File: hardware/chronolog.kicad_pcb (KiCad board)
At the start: 2 copper layers, 100 x 50 mm, 92 parts, among them J1 DC-005-5A-2.0, J2 B4B-XH-A, J3 B-2100S04P-A110, J4 U254-051N-4BH806, Q1 BSS138, Q2 BSS138, Q3 BC817-40LT1G, U1 AP63205WU-7, U2 STM32F072CBT6, U3 AP2114H-3.3TRG1, U4 USBLC6-2SC6, U5 W25Q32JVSNIQ, U6 LM75BD, U7 ESP-01, U8 WC1602A, U9 PCF8574T, Y1 32.768kHz

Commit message: hardware(feat): configure board stackup and design rules
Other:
- copper layers 2 -> 4
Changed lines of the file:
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@@
 	(generator_version "9.0")
 	(general
-		(thickness 1.6)
+		(thickness 1.6062)
 		(legacy_teardrops no)
 	)
@@
 	(layers
 		(0 "F.Cu" signal)
+		(4 "In1.Cu" signal)
+		(6 "In2.Cu" signal)
 		(2 "B.Cu" signal)
 		(9 "F.Adhes" user "F.Adhesive")
@@
 	)
 	(setup
+		(stackup
+			(layer "F.SilkS"
+				(type "Top Silk Screen")
+			)
+			(layer "F.Paste"
+				(type "Top Solder Paste")
+			)
+			(layer "F.Mask"
+				(type "Top Solder Mask")
+				(thickness 0.01)
+			)
+			(layer "F.Cu"
+				(type "copper")
+				(thickness 0.035)
+			)
+			(layer "dielectric 1"
+				(type "prepreg")
+				(thickness 0.2104)
+				(material "FR4")
+				(epsilon_r 4.5)
+				(loss_tangent 0.02)
+			)
+			(layer "In1.Cu"
+				(type "copper")
+				(thickness 0.0152)
+			)
+			(layer "dielectric 2"
+				(type "core")
+				(thickness 1.065)
+				(material "FR4")
+				(epsilon_r 4.5)
+				(loss_tangent 0.02)
+			)
+			(layer "In2.Cu"
+				(type "copper")
+				(thickness 0.0152)
+			)
+			(layer "dielectric 3"
+				(type "prepreg")
+				(thickness 0.2104)
+				(material "FR4")
+				(epsilon_r 4.5)
+				(loss_tangent 0.02)
+			)
+			(layer "B.Cu"
+				(type "copper")
+				(thickness 0.035)
+			)
+			(layer "B.Mask"
+				(type "Bottom Solder Mask")
+				(thickness 0.01)
+			)
+			(layer "B.Paste"
+				(type "Bottom Solder Paste")
+			)
+			(layer "B.SilkS"
+				(type "Bottom Silk Screen")
+			)
+			(copper_finish "None")
+			(dielectric_constraints no)
+		)
 		(pad_to_mask_clearance 0)
 		(allow_soldermask_bridges_in_footprints no)

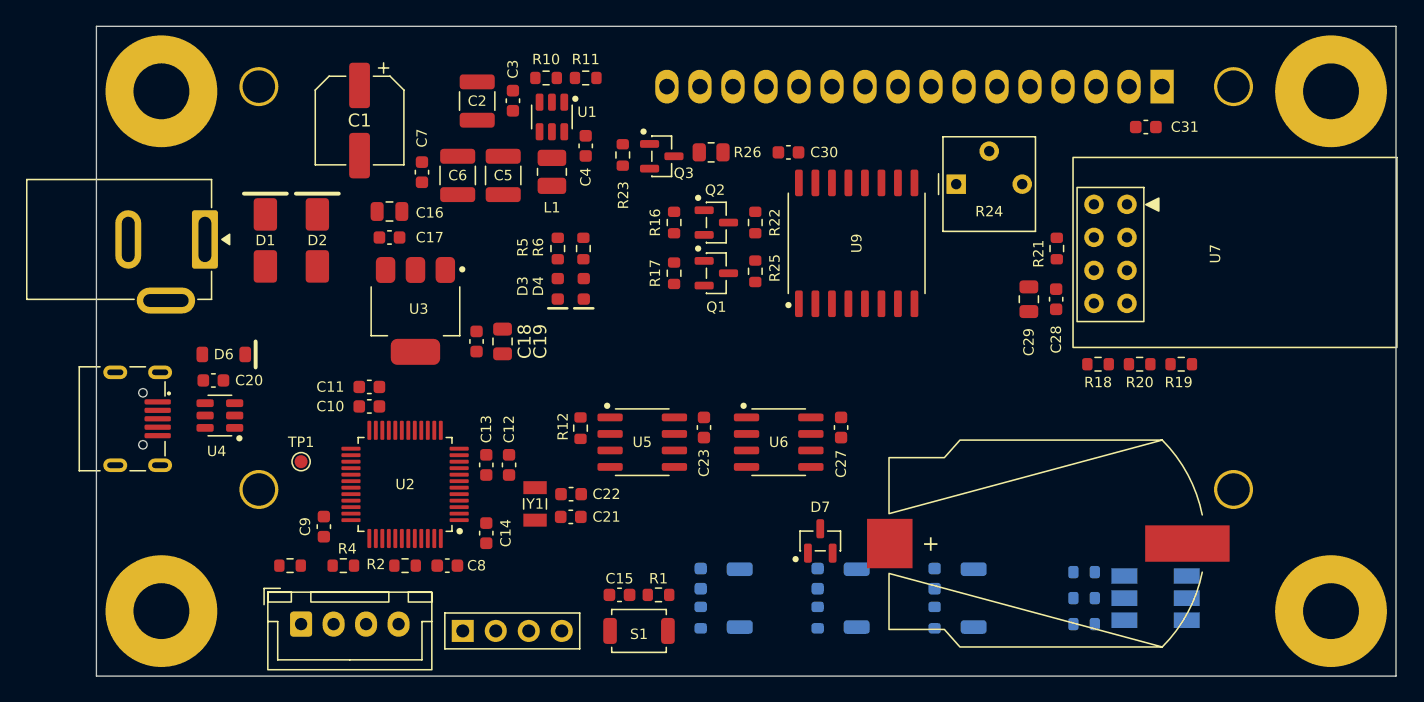
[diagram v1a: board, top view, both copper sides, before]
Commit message: hardware(feat): route simple connections
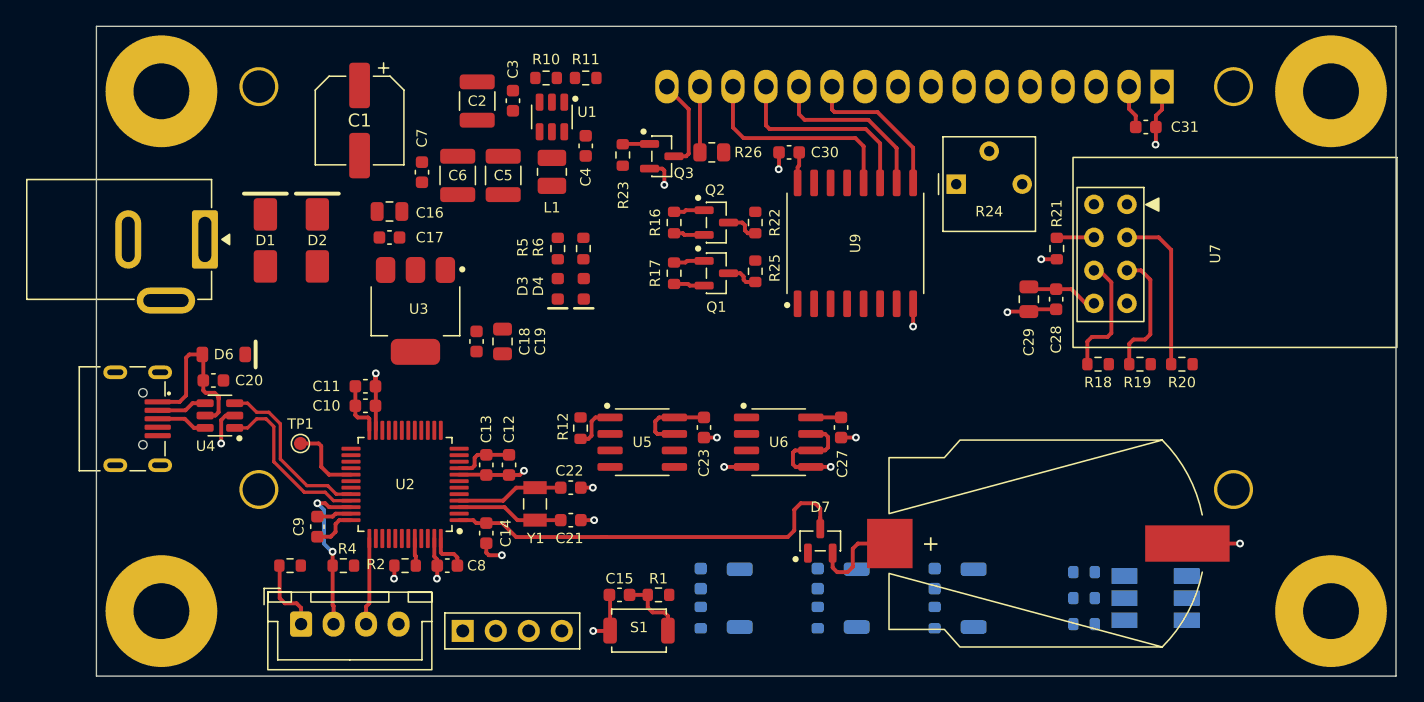
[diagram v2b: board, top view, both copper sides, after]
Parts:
- moved R20 3.25 mm to (182.0, 106.0)
- moved R19 3.17 mm to (178.8, 106.0)
- moved TP1 1.40 mm to (114.2, 112.1)
- moved C22 0.50 mm to (135.0, 115.5)
- moved C9 0.50 mm to (115.5, 118.5)
- moved C10 0.30 mm to (119.2, 109.2)
- moved C11 0.30 mm to (119.2, 107.7)
- moved C21 0.25 mm to (135.0, 118.0)
- moved U9 0.10 mm to (156.9, 96.7)
- moved R26 0.05 mm to (145.9, 89.7)
- moved C30 0.05 mm to (151.8, 89.7)
- turned S1 to 0 degrees
- turned R3 to 0 degrees
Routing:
- net GND: track 0.00 -> 60.5 mm, vias 0 -> 20
- net +3V3: track 0.00 -> 34.5 mm
- net +VBAT: track 0.00 -> 33.2 mm
- net /[08] - LCD/LCD_D7: track 0.00 -> 16.6 mm
- net /[08] - LCD/LCD_D6: track 0.00 -> 15.4 mm
- net /[04] - MCU/USB_D_P: track 0.00 -> 13.4 mm
- net /[04] - MCU/USB_D_N: track 0.00 -> 13.4 mm
- net /[08] - LCD/LCD_D5: track 0.00 -> 13.4 mm
- net +VBUS: track 0.00 -> 13.4 mm
- net /[04] - MCU/SWDIO: track 0.00 -> 12.7 mm, vias 0 -> 2
- net Net-(U7-IO2): track 0.00 -> 12.6 mm
- net /[08] - LCD/LCD_D4: track 0.00 -> 11.9 mm
- net Net-(U7-IO0): track 0.00 -> 9.80 mm
- net Net-(U7-~{RST}): track 0.00 -> 9.49 mm
- net /[04] - MCU/OSC32_OUT: track 0.00 -> 8.23 mm
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- added copper zone on In1.Cu, net GND

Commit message: hardware(feat): route power supply
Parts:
- moved C1 0.75 mm to (118.0, 87.2)
- moved C16 0.25 mm to (121.1, 94.5)
- moved C17 0.25 mm to (121.1, 96.5)
- moved C4 0.16 mm to (136.2, 89.3)
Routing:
- net +5V: track 5.72 -> 18.5 mm, vias 0 -> 6
- net Net-(D1-A): track 0.00 -> 10.3 mm
- net Net-(U1-SW): track 0.00 -> 4.61 mm
- net GND: track 60.5 -> 64.3 mm, vias 20 -> 37
- net Net-(U1-EN): track 0.00 -> 3.42 mm
- net Net-(U1-BST): track 0.00 -> 2.79 mm
- net Net-(D4-A): track 0.00 -> 1.50 mm
- net Net-(D3-A): track 0.00 -> 1.49 mm
- net +3V3: vias 0 -> 4
- added copper zone on F.Cu, net +12V
- added copper zone on F.Cu, net +3V3
- added copper zone on F.Cu, net +5V
- added copper zone on F.Cu, net GND

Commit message: hardware(feat): place internal zones +5V and +3V3
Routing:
- net +3V3: track 34.5 -> 51.5 mm, vias 4 -> 16
- net GND: track 64.3 -> 69.1 mm, vias 37 -> 40
- net +5V: track 18.5 -> 21.8 mm, vias 6 -> 10
- added copper zone on In2.Cu, net +3V3
- added copper zone on In2.Cu, net +5V

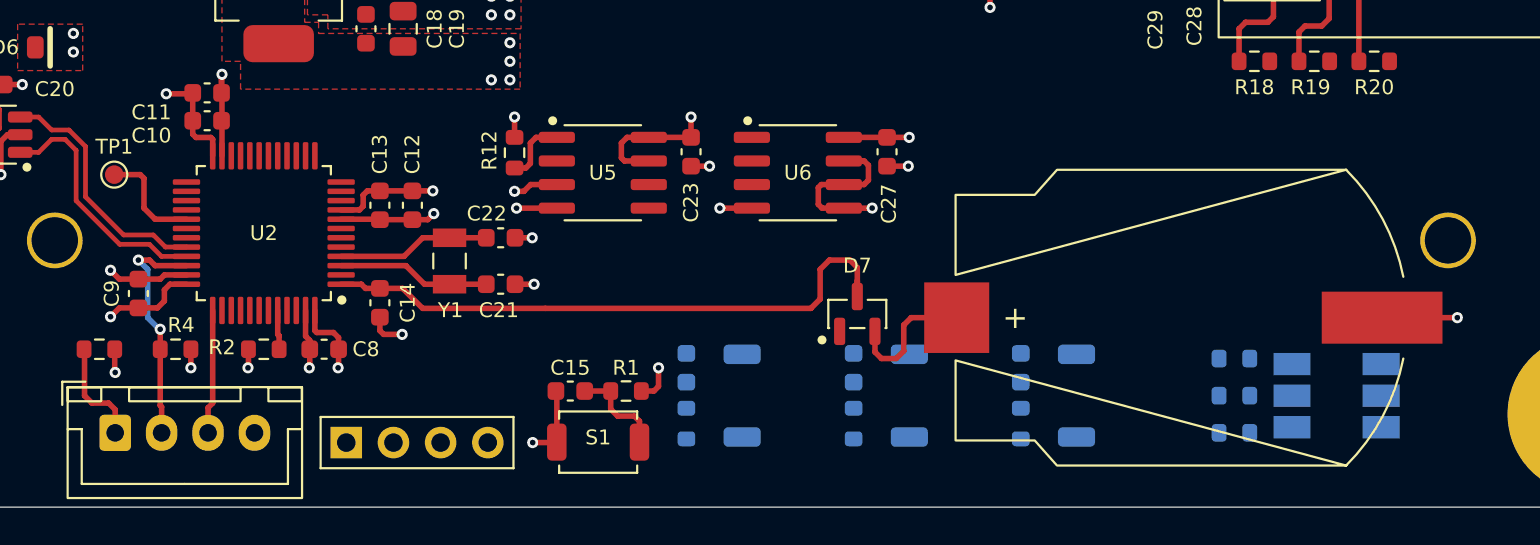
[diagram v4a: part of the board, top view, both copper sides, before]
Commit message: hardware(feat): route main button, leds and nor connections
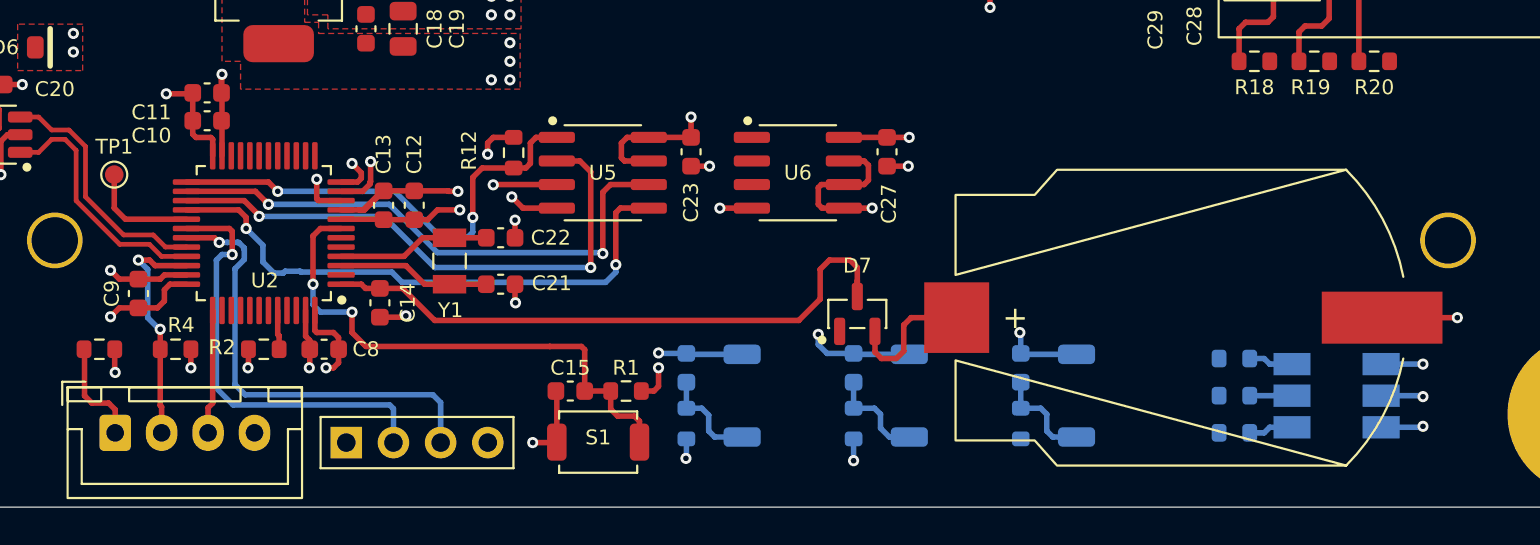
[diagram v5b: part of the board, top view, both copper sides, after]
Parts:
- moved C13 0.20 mm to (128.7, 113.8)
- moved C12 0.10 mm to (130.3, 113.8)
- moved R12 0.05 mm to (135.7, 110.9)
- turned R7 to 0 degrees
- turned R9 to 0 degrees
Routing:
- net SPI2_MOSI: track 0.00 -> 31.1 mm, vias 0 -> 2
- net SPI2_MISO: track 0.00 -> 30.5 mm, vias 0 -> 2
- net SPI2_SCK: track 0.00 -> 29.7 mm, vias 0 -> 2
- net /[04] - MCU/USART1_RX: track 0.00 -> 24.5 mm, vias 0 -> 1
- net /[04] - MCU/~{NRST}: track 5.34 -> 29.2 mm, vias 0 -> 2
- net /[04] - MCU/USART1_TX: track 0.00 -> 23.5 mm, vias 0 -> 1
- net GND: track 69.1 -> 91.6 mm, vias 40 -> 46
- net SPI2_NSS: track 3.60 -> 25.7 mm, vias 0 -> 2
- net BUTTON2: track 0.00 -> 8.48 mm, vias 0 -> 1
- net BUTTON1: track 0.00 -> 7.97 mm, vias 0 -> 1
- net BUTTON3: track 0.00 -> 7.66 mm, vias 0 -> 1
- net +3V3: track 51.5 -> 59.1 mm, vias 16 -> 18
- net Net-(D5-GA): track 0.00 -> 2.40 mm
- net Net-(D5-BA): track 0.00 -> 2.40 mm
- net Net-(D5-RA): track 0.00 -> 2.28 mm
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
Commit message: hardware(feat): connect all items in pcb
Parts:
- moved C18 2.25 mm to (127.8, 102.0)
- moved C19 2.25 mm to (129.8, 102.0)
- moved C21 1.12 mm to (136.1, 118.0)
- moved C22 1.12 mm to (136.1, 115.5)
- moved Y1 1.12 mm to (133.4, 116.8)
- moved C12 0.99 mm to (131.0, 114.5)
- moved C13 0.99 mm to (129.3, 114.5)
- moved C23 0.90 mm to (146.2, 110.9)
- moved R12 0.90 mm to (136.6, 110.9)
- moved U5 0.90 mm to (141.4, 112.0)
- moved U6 0.90 mm to (151.9, 112.0)
- moved C27 0.90 mm to (156.7, 110.9)
- moved C10 0.64 mm to (118.8, 108.7)
- moved C11 0.64 mm to (118.8, 107.2)
- moved R24 0.41 mm to (167.1, 92.4)
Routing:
- net USART3_RX: track 0.00 -> 75.0 mm, vias 0 -> 1
- net /[04] - MCU/LED_GREEN: track 0.00 -> 73.0 mm, vias 0 -> 1
- net /[04] - MCU/LED_BLUE: track 0.00 -> 70.5 mm, vias 0 -> 1
- net ESP_EN: track 2.87 -> 72.7 mm, vias 0 -> 2
- net USART3_TX: track 0.00 -> 69.6 mm, vias 0 -> 1
- net I2C1_SDA: track 2.36 -> 71.7 mm, vias 0 -> 4
- net /[04] - MCU/LED_RED: track 0.00 -> 68.5 mm, vias 0 -> 1
- net I2C1_SCL: track 2.36 -> 65.1 mm, vias 0 -> 4
- net BUTTON2: track 8.48 -> 71.0 mm
- net BUTTON3: track 7.66 -> 64.4 mm
- net BUTTON1: track 7.97 -> 60.6 mm
- net +3V3: track 59.1 -> 99.2 mm, vias 18 -> 26
- net /[08] - LCD/LCD_BL: track 0.00 -> 33.2 mm, vias 0 -> 2
- net /[08] - LCD/LCD_RS: track 0.00 -> 29.8 mm, vias 0 -> 1
- net /[08] - LCD/LCD_RW: track 0.00 -> 26.0 mm, vias 0 -> 1
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
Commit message: hardware(feat): improve route
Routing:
- net /[08] - LCD/LCD_BL: track 33.2 -> 43.3 mm
- net I2C1_SDA: track 71.7 -> 75.2 mm
- net I2C1_SCL: track 65.1 -> 68.4 mm
- net BUTTON2: track 71.0 -> 70.5 mm
- net USART3_TX: track 69.6 -> 70.1 mm

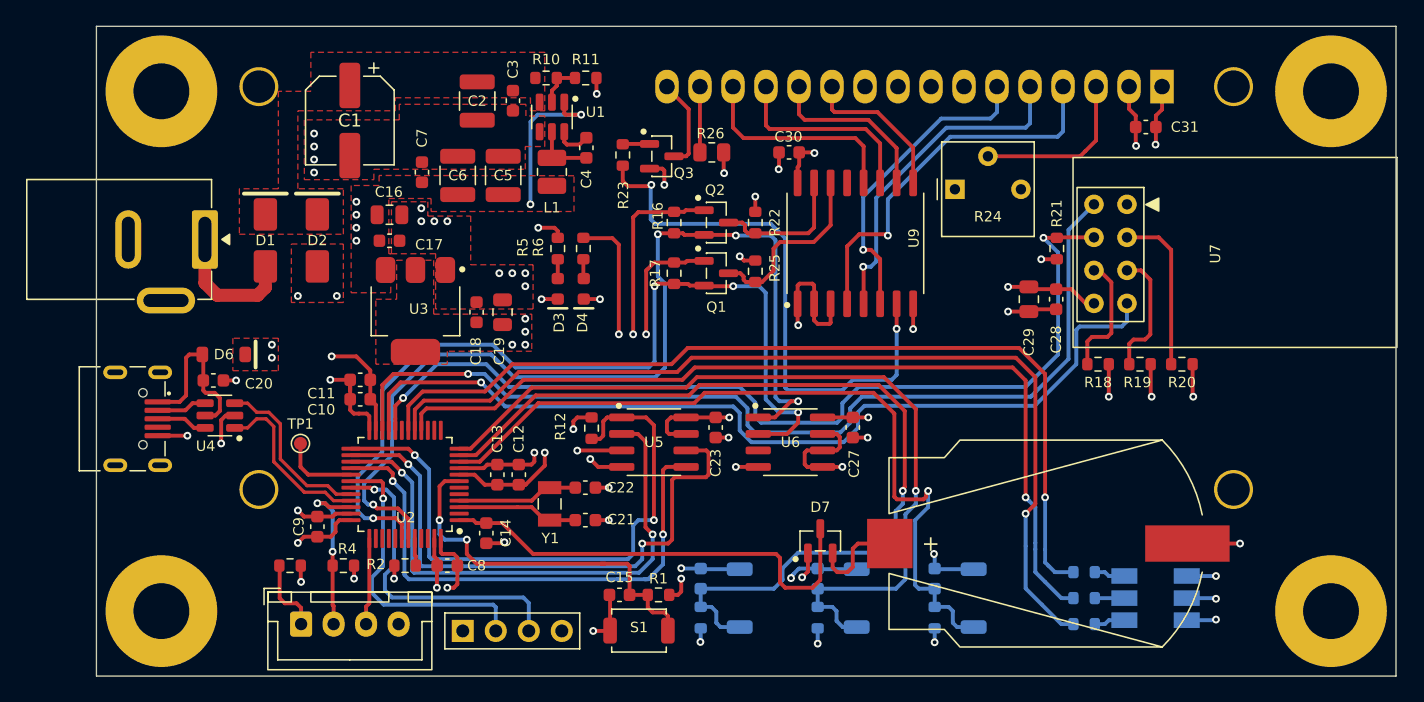
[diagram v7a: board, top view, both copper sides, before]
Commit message: hardware(feat): place logos and pcb project name
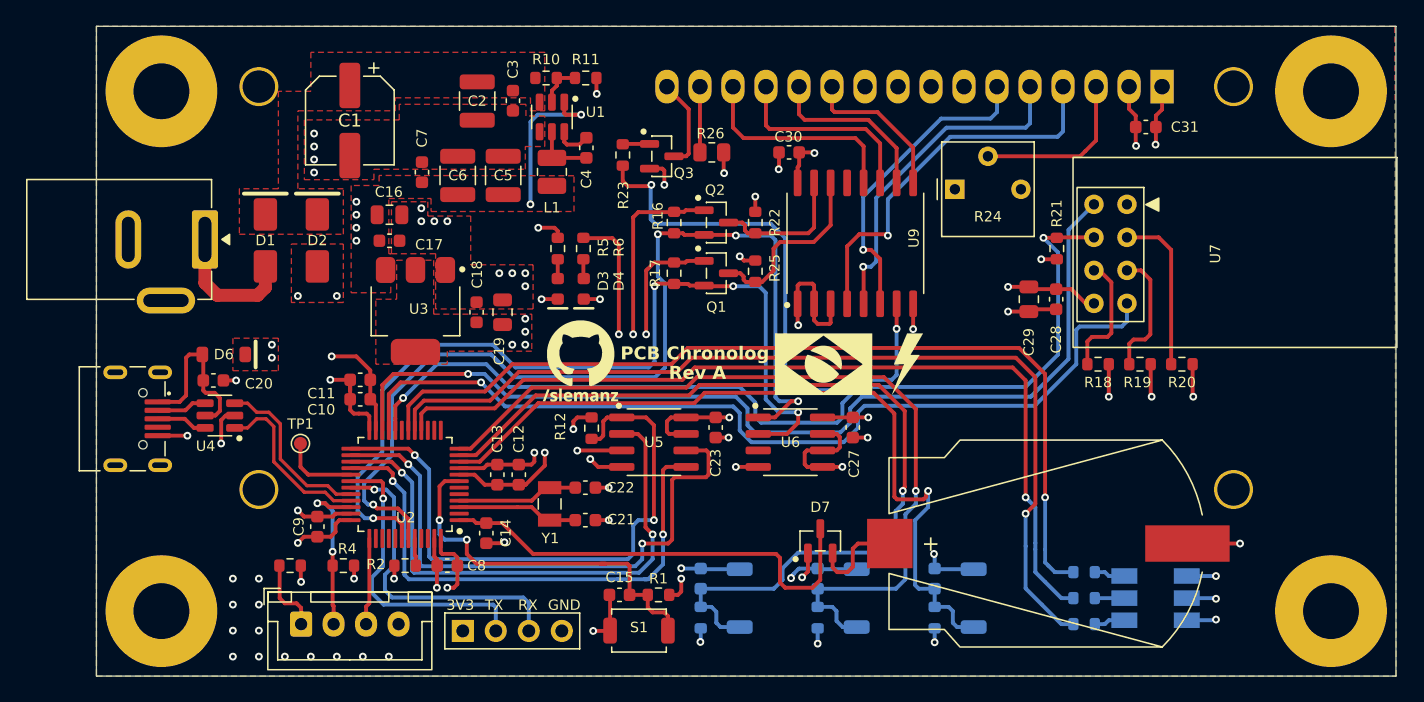
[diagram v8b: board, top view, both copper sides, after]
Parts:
- added REF**: LOGO_Slemanz_GitHub_5.8x6.25mm, 12_mechanical:LOGO_Slemanz_GitHub_5.8x6.25mm, F.Cu at (135.8, 105.8)
- added REF**: LOGO_Storm_2.4x4.75mm, 12_mechanical:LOGO_Storm_2.4x4.75mm, F.Cu at (160.9, 106.0)
- added REF**: LOGO_Brasil_Flag_7.5x4.75mm, 12_mechanical:LOGO_Brasil_Flag_7.5x4.75mm, F.Cu at (154.4, 106.0)
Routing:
- net GND: vias 48 -> 61
- added copper zone on B.Cu, net GND
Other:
- board text added: "3V3"
- board text added: "GND"
- board text added: "PCB Chronolog"
- board text added: "RX"
- board text added: "Rev A"
- board text added: "TX"
